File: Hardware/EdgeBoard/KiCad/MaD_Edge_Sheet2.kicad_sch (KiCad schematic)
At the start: 101 parts, among them IC1 ISO6742DWR, IC10 NSI50010YT1G, IC11 NSI50010YT1G, IC12 NSI50010YT1G, IC13 NSI50010YT1G, IC2 ISO6742DWR, IC3 UCC12040DVER, IC4 UCC12040DVER, IC5 ISO6731DWR, IC6 NSI50010YT1G, IC7 NSI50010YT1G, IC8 NSI50010YT1G, IC9 NSI50010YT1G, J10 ChargePump, J11 ESDUpper, J12 ESDLower, J13 ESDActive, J14 ENDUpper, J15 ENDLower, J16 Door, J17 GPI_3, J18 GPI_4, J19 NavKey, J4 436500321, J5 GPO_2, J6 GPO_1, J7 GPI_2, J8 GPI_1, J9 Force, U10 SN74LVC1G14DBV, U11 SN74LVC1G14DBV, U12 SN74LVC1G14DBV, U13 SN74LVC1G14DBV, U14 SN74LVC1G14DBV, U15 SN74LVC1G14DBV, U16 SN74LVC1G14DBV, U17 SN74LVC1G14DBV, U18 SN74LVC1G14DBV, U19 SN74LVC1G14DBV, U21 SN74LVC1G14DBV, U22 SN74LVC1G14DBV, U4 6N137, U5 VO2631, U6 VO2631, U7 VO2631, U8 VO2631, U9 SN74LVC1G14DBV

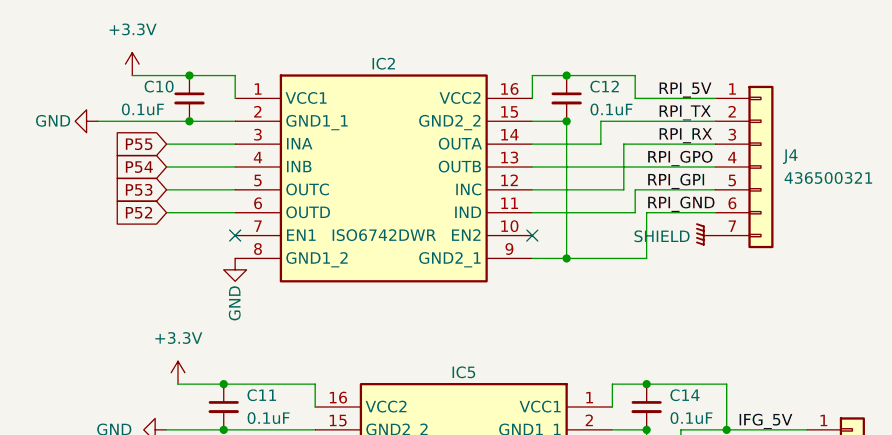
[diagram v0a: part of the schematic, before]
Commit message: fix(hardware): Pi link on P29-P32 and a 3.3 V Pi side
Findings HOST-F2 and HOST-F5. The P2-EC32MB does not bring out P40-P57
(fingers 59-62 are no-connects), so IC2 on P52-P55 was dead, and the Pi
side ran from 5 V, putting about 5 V on Pi GPIO.

- IC2 INA/INB/OUTC/OUTD move to P32/P31/P30/P29. P29-P31 are the only
  EC32MB pins the carrier leaves unused; the fourth (an isolator input,
  10 uA max, SLLSFJ6G p.12) shares P32 with J22.3.
- Routes: the old P52-P55 copper is removed; IC2 to four vias, B.Cu down
  to J22.3 (P32) and to vias in J3 fingers 9-11 (the only access).
- RPI_5V renamed RPI_3V3 (pads, tracks, In2 plane); J4.1 silkscreen
  reads 3V3. ISO674x runs at 2.25-5.5 V with VIT+ = 0.7 VCCI (SLLSFJ6G
  p.8, p.12).
- IC2 alternate ISO7742FDWR dropped: a default-low output would hold the
  UART low (SLLSFJ6G p.31).

Firmware follow-up: HW_PIN_RPI_TX 55 -> 32, HW_PIN_RPI_RX 53 -> 30.

Co-Authored-By: Claude Opus 5.5 <noreply@anthropic.com>
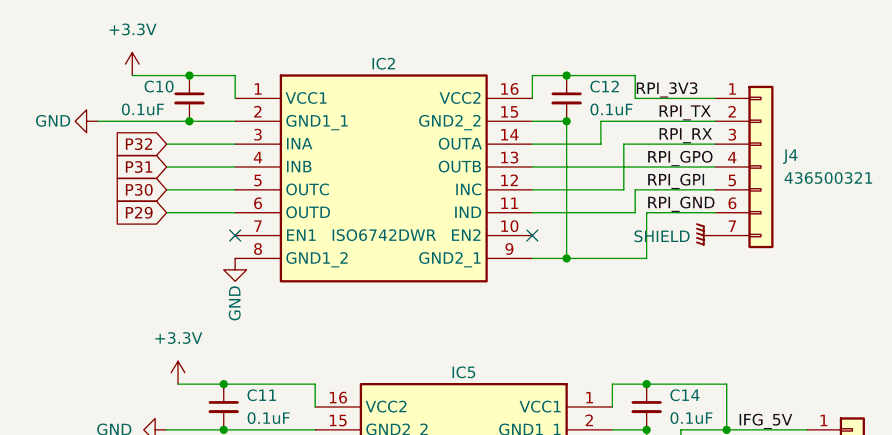
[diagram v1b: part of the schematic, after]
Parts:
- IC2: NOTES Pin Compatible with ISO77xx -> Non-F (default-high) part only: UART lines idle high. VCC2 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; manufacturer_part_number_1 ISO6742DWR or ISO7742FDWR -> ISO6742DWR
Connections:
- net P52 renamed P29
- net P53 renamed P30
- net P54 renamed P31
- net P55 renamed P32
- net RPI_5V renamed RPI_3V3
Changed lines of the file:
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@@
 		)
 	)
-	(label "RPI_5V"
-		(at 85.09 21.59 0)
+	(label "RPI_3V3"
+		(at 82.55 21.59 0)
 		(effects
 			(font
@@
 		)
 	)
-	(global_label "P52"
+	(global_label "P29"
 		(shape input)
 		(at 30.48 34.29 180)
@@
 		)
 	)
-	(global_label "P54"
+	(global_label "P31"
 		(shape input)
 		(at 30.48 29.21 180)
@@
 		)
 	)
-	(global_label "P55"
+	(global_label "P32"
 		(shape input)
 		(at 30.48 26.67 180)
@@
 		)
 	)
-	(global_label "P53"
+	(global_label "P30"
 		(shape input)
 		(at 30.48 31.75 180)
@@
 			)
 		)
-		(property "NOTES" "Pin Compatible with ISO77xx"
+		(property "NOTES" "Non-F (default-high) part only: UART lines idle high. VCC2 = RPI_3V3 from the Pi 3.3 V pin (VCC 2.25-5.5 V, SLLSFJ6G)."
 			(at 38.1 21.59 0)
 			(effects
@@
 			)
 		)
-		(property "manufacturer_part_number_1" "ISO6742DWR or ISO7742FDWR"
+		(property "manufacturer_part_number_1" "ISO6742DWR"
 			(at 38.1 21.59 0)
 			(effects

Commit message: fix(hardware): J4 back on the 43045-0618 footprint
Finding HOST-J4. J4's BOM part is 0430450618 (with solder tabs) and the
2023 board used the 43045-0618 footprint; the current files had 0615
(no tabs). The library footprint drops in at the same place: its two
mounting pads clear all copper (checked against every F.Cu item with
0.2 mm clearance). The tabs stay unnumbered as in 2023, so the DRC
parity note about J4 pin 7 (SHIELD) is unchanged.

Co-Authored-By: Claude Opus 5.5 <noreply@anthropic.com>
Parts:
- J4: footprint Connector_Molex:Molex_Micro-Fit_3.0_43045-0615_2x03_P3.00mm_Vertical -> Connector_Molex:Molex_Micro-Fit_3.0_43045-0618_2x03-1MP_P3.00mm_Vertical
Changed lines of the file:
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@@
 			)
 		)
-		(property "Footprint" "Connector_Molex:Molex_Micro-Fit_3.0_43045-0615_2x03_P3.00mm_Vertical"
+		(property "Footprint" "Connector_Molex:Molex_Micro-Fit_3.0_43045-0618_2x03-1MP_P3.00mm_Vertical"
 			(at 96.52 29.21 0)
 			(effects

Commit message: docs(hardware): Edge carrier revision v0.3: marking and changelog
- Title blocks (three sheets and the PCB) and the silkscreen read v0.3.
- readme: the v0.3 changelog (each change, the finding, the datasheet
  cite), encoder jumper settings for RS-422, open-collector and push-pull
  encoders, the supported loop range, J1 as the host port, the P2-EC32MB
  pin facts, the J3 via-in-pad fab note, and the firmware/SIL follow-up.

Co-Authored-By: Claude Opus 5.5 <noreply@anthropic.com>
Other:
- company: (none) -> MaD
- title: (none) -> MaD Edge carrier: I/O and host link
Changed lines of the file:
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@@
 	(generator_version "9.0")
 	(paper "A4")
+	(title_block
+		(title "MaD Edge carrier: I/O and host link")
+		(date "2026-10-25")
+		(rev "v0.3")
+		(company "MaD")
+		(comment 1 "Revision v0.3: fixes from the SIL hardware findings; see Hardware/EdgeBoard/readme.md")
+	)
 	(text "5V"
 		(exclude_from_sim no)

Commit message: fix(hardware): IC1/IC2 order the non-F ISO6742DWR (LCSC C5216407)
Both isolators carried LCSC C2862403, which LCSC's product detail lists as
the ISO7742FDWR (measured). That is the default-low F part: on IC2 it would
hold the Pi's RX low (a break) whenever the P2 is in reset or not driving
P32, and hold P30 low with no Pi attached (SLLSFJ6G function table).

C5216407 is the TI ISO6742DWR (LCSC product detail, measured), the part
both symbols are drawn as and the one the DigiKey number names. IC1 follows
IC2 into the same row and drops its ISO7742FDWR alternate. The firmware
does not drive P24-P27 (no HW_pins.h entry), so IC1's outputs change only
in what an unused channel idles at.

Fields only; no connectivity change.

Co-Authored-By: Claude Opus 5.5 <noreply@anthropic.com>
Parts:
- IC1: LCSC C2862403 -> C5216407; NOTES Pin Compatible with ISO77xx -> Pin compatible with ISO77xx. Ordered as the non-F ISO6742DW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; manufacturer_part_number_1 ISO6742DWR or ISO7742FDWR -> ISO6742DWR
- IC2: LCSC C2862403 -> C5216407
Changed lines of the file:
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@@
 			)
 		)
-		(property "LCSC" "C2862403"
+		(property "LCSC" "C5216407"
 			(at 38.1 21.59 0)
 			(effects
@@
 			)
 		)
-		(property "LCSC" "C2862403"
+		(property "LCSC" "C5216407"
 			(at 36.83 134.62 0)
 			(effects
@@
 			)
 		)
-		(property "NOTES" "Pin Compatible with ISO77xx"
+		(property "NOTES" "Pin compatible with ISO77xx. Ordered as the non-F ISO6742DWR (LCSC C5216407): outputs idle high while the input side is unpowered or undriven (SLLSFJ6G)."
 			(at 36.83 134.62 0)
 			(effects
@@
 			)
 		)
-		(property "manufacturer_part_number_1" "ISO6742DWR or ISO7742FDWR"
+		(property "manufacturer_part_number_1" "ISO6742DWR"
 			(at 36.83 134.62 0)
 			(effects

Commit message: fix(hardware): BOM fields for F1, the 0.1 uF row, the shunts and J25
- F1: LCSC C7542932 is the LUTE 1206L020/30NR (LCSC product detail,
  measured): 0.20 A hold, 0.46 A trip, 30 V (LUTE 1206L datasheet, Revision
  2020, p.2). Manufacturer, trip current and datasheet link now say so.
- The 0.1 uF 0603 row (22 parts, C31 among them) orders LCSC C14663, the
  YAGEO CC0603KRX7R9BB104, 50 V X7R 0603 (LCSC product detail, measured).
  Its primary MPN was a Samsung 0402 part (CL05A104KA5NNNC) with a 6 V
  description. The MPN, manufacturer and description now match the ordered
  part; the DigiKey number that went with the Samsung MPN is cleared
  because it could not be checked.
- SH1-SH4: noted as hand-fit after assembly (no footprint, no CPL entry).
- IC14: note to check the ISO7741F top marking on receipt (SLLSEP4K
  package addendum p.38), since LCSC's parametric text for C485810 calls
  its fail-safe state high.
- J25: VIN is the encoder's own rated supply, 30 V max (F1), isolated from
  V_IN.

Fields only; no connectivity change.

Co-Authored-By: Claude Opus 5.5 <noreply@anthropic.com>
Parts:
- C10, C11, C12, C13, C14, C15, C18, C19, C20, C21, C22, C23, C7, C8, C9: DIGIKEY 1276-1043-1-ND -> (none); MANUFACTURER Samsung Electro-Mechanics -> YAGEO; Manufacturer_Part_Number CL05A104KA5NNNC -> CC0603KRX7R9BB104
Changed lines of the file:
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@@
 			)
 		)
-		(property "Description" "0.1uF 6V SMD"
+		(property "Description" "0.1uF 50V X7R 0603"
 			(at 29.21 171.45 0)
 			(effects
@@
 			)
 		)
-		(property "MANUFACTURER" "Samsung Electro-Mechanics"
+		(property "MANUFACTURER" "YAGEO"
 			(at 29.21 171.45 0)
 			(effects
@@
 			)
 		)
-		(property "Manufacturer_Part_Number" "CL05A104KA5NNNC"
+		(property "Manufacturer_Part_Number" "CC0603KRX7R9BB104"
 			(at 29.21 171.45 0)
 			(effects
@@
 			)
 		)
-		(property "DIGIKEY" "1276-1043-1-ND"
+		(property "DIGIKEY" ""
 			(at 29.21 171.45 0)
 			(effects
@@
 			)
 		)
-		(property "Description" "0.1uF 6V SMD"
+		(property "Description" "0.1uF 50V X7R 0603"
 			(at 83.82 81.28 0)
 			(effects
@@
 			)
 		)
-		(property "MANUFACTURER" "Samsung Electro-Mechanics"
+		(property "MANUFACTURER" "YAGEO"
 			(at 83.82 81.28 0)
 			(effects
@@
 			)
 		)
-		(property "Manufacturer_Part_Number" "CL05A104KA5NNNC"
+		(property "Manufacturer_Part_Number" "CC0603KRX7R9BB104"
 			(at 83.82 81.28 0)
 			(effects
@@
 			)
 		)
-		(property "DIGIKEY" "1276-1043-1-ND"
+		(property "DIGIKEY" ""
 			(at 83.82 81.28 0)
 			(effects
@@
 			)
 		)
-		(property "Description" "0.1uF 6V SMD"
+		(property "Description" "0.1uF 50V X7R 0603"
 			(at 97.79 176.53 0)
 			(effects
@@
 			)
 		)
-		(property "MANUFACTURER" "Samsung Electro-Mechanics"
+		(property "MANUFACTURER" "YAGEO"
 			(at 97.79 176.53 0)
 			(effects
@@
 			)
 		)
-		(property "Manufacturer_Part_Number" "CL05A104KA5NNNC"
+		(property "Manufacturer_Part_Number" "CC0603KRX7R9BB104"
 			(at 97.79 176.53 0)
 			(effects
@@
 			)
 		)
-		(property "DIGIKEY" "1276-1043-1-ND"
+		(property "DIGIKEY" ""
 			(at 97.79 176.53 0)
 			(effects
@@
 			)
 		)
-		(property "Description" "0.1uF 6V SMD"
+		(property "Description" "0.1uF 50V X7R 0603"
 			(at 154.94 20.32 0)
 			(effects
@@
 			)
 		)
-		(property "MANUFACTURER" "Samsung Electro-Mechanics"
+		(property "MANUFACTURER" "YAGEO"
 			(at 154.94 20.32 0)
 			(effects
@@
 			)
 		)
-		(property "Manufacturer_Part_Number" "CL05A104KA5NNNC"
+		(property "Manufacturer_Part_Number" "CC0603KRX7R9BB104"
 			(at 154.94 20.32 0)
 			(effects
@@
 			)
 		)
-		(property "DIGIKEY" "1276-1043-1-ND"
+		(property "DIGIKEY" ""
 			(at 154.94 20.32 0)
 			(effects
@@
 			)
 		)
-		(property "Description" "0.1uF 6V SMD"
+		(property "Description" "0.1uF 50V X7R 0603"
 			(at 154.94 58.42 0)
 			(effects
@@
 			)
 		)
-		(property "MANUFACTURER" "Samsung Electro-Mechanics"
+		(property "MANUFACTURER" "YAGEO"
 			(at 154.94 58.42 0)
 			(effects
@@
 			)
 		)
-		(property "Manufacturer_Part_Number" "CL05A104KA5NNNC"
+		(property "Manufacturer_Part_Number" "CC0603KRX7R9BB104"
 			(at 154.94 58.42 0)
 			(effects
@@
 			)
 		)
-		(property "DIGIKEY" "1276-1043-1-ND"
+		(property "DIGIKEY" ""
 			(at 154.94 58.42 0)
 			(effects
@@
 			)
 		)
-		(property "Description" "0.1uF 6V SMD"
+		(property "Description" "0.1uF 50V X7R 0603"
 			(at 78.74 134.62 0)
 			(effects
@@
 			)
 		)
-		(property "MANUFACTURER" "Samsung Electro-Mechanics"
+		(property "MANUFACTURER" "YAGEO"
 			(at 78.74 134.62 0)
 			(effects
@@
 			)
 		)
-		(property "Manufacturer_Part_Number" "CL05A104KA5NNNC"
+		(property "Manufacturer_Part_Number" "CC0603KRX7R9BB104"
 			(at 78.74 134.62 0)
 			(effects
@@
 			)
 		)
-		(property "DIGIKEY" "1276-1043-1-ND"
+		(property "DIGIKEY" ""
 			(at 78.74 134.62 0)
 			(effects
@@
 			)
 		)
-		(property "Description" "0.1uF 6V SMD"
+		(property "Description" "0.1uF 50V X7R 0603"
 			(at 36.83 55.88 0)
 			(effects
@@
 			)
 		)
-		(property "MANUFACTURER" "Samsung Electro-Mechanics"
+		(property "MANUFACTURER" "YAGEO"
 			(at 36.83 55.88 0)
 			(effects
@@
 			)
 		)
-		(property "Manufacturer_Part_Number" "CL05A104KA5NNNC"
+		(property "Manufacturer_Part_Number" "CC0603KRX7R9BB104"
 			(at 36.83 55.88 0)
 			(effects
@@
 			)
 		)
-		(property "DIGIKEY" "1276-1043-1-ND"
+		(property "DIGIKEY" ""
 			(at 36.83 55.88 0)
 			(effects
@@
 			)
 		)
-		(property "Description" "0.1uF 6V SMD"
+		(property "Description" "0.1uF 50V X7R 0603"
 			(at 31.75 90.17 0)
 			(effects
@@
 			)
 		)
-		(property "MANUFACTURER" "Samsung Electro-Mechanics"
+		(property "MANUFACTURER" "YAGEO"
 			(at 31.75 90.17 0)
 			(effects
@@
 			)
 		)
-		(property "Manufacturer_Part_Number" "CL05A104KA5NNNC"
+		(property "Manufacturer_Part_Number" "CC0603KRX7R9BB104"
 			(at 31.75 90.17 0)
 			(effects
@@
 			)
 		)
-		(property "DIGIKEY" "1276-1043-1-ND"
+		(property "DIGIKEY" ""
 			(at 31.75 90.17 0)
 			(effects
@@
 			)
 		)
-		(property "Description" "0.1uF 6V SMD"
+		(property "Description" "0.1uF 50V X7R 0603"
 			(at 74.93 21.59 0)
 			(effects
@@
 			)
 		)
-		(property "MANUFACTURER" "Samsung Electro-Mechanics"
+		(property "MANUFACTURER" "YAGEO"
 			(at 74.93 21.59 0)
 			(effects
@@
 			)
 		)
-		(property "Manufacturer_Part_Number" "CL05A104KA5NNNC"
+		(property "Manufacturer_Part_Number" "CC0603KRX7R9BB104"
 			(at 74.93 21.59 0)
 			(effects
@@
 			)
 		)
-		(property "DIGIKEY" "1276-1043-1-ND"
+		(property "DIGIKEY" ""
 			(at 74.93 21.59 0)
 			(effects
@@
 			)
 		)
-		(property "Description" "0.1uF 6V SMD"
+		(property "Description" "0.1uF 50V X7R 0603"
 			(at 31.75 134.62 0)
 			(effects
@@
 			)
 		)
-		(property "MANUFACTURER" "Samsung Electro-Mechanics"
+		(property "MANUFACTURER" "YAGEO"
 			(at 31.75 134.62 0)
 			(effects
@@
 			)
 		)
-		(property "Manufacturer_Part_Number" "CL05A104KA5NNNC"
+		(property "Manufacturer_Part_Number" "CC0603KRX7R9BB104"
 			(at 31.75 134.62 0)
 			(effects
@@
 			)
 		)
-		(property "DIGIKEY" "1276-1043-1-ND"
+		(property "DIGIKEY" ""
 			(at 31.75 134.62 0)
 			(effects
@@
 			)
 		)
-		(property "Description" "0.1uF 6V SMD"
+		(property "Description" "0.1uF 50V X7R 0603"
 			(at 83.82 55.88 0)
 			(effects
@@
 			)
 		)
-		(property "MANUFACTURER" "Samsung Electro-Mechanics"
+		(property "MANUFACTURER" "YAGEO"
 			(at 83.82 55.88 0)
 			(effects
@@
 			)
 		)
-		(property "Manufacturer_Part_Number" "CL05A104KA5NNNC"
+		(property "Manufacturer_Part_Number" "CC0603KRX7R9BB104"
 			(at 83.82 55.88 0)
 			(effects
@@
 			)
 		)
-		(property "DIGIKEY" "1276-1043-1-ND"
+		(property "DIGIKEY" ""
 			(at 83.82 55.88 0)
 			(effects
@@
 			)
 		)
-		(property "Description" "0.1uF 6V SMD"
+		(property "Description" "0.1uF 50V X7R 0603"
 			(at 133.35 182.88 0)
 			(effects
@@
 			)
 		)
-		(property "MANUFACTURER" "Samsung Electro-Mechanics"
+		(property "MANUFACTURER" "YAGEO"
 			(at 133.35 182.88 0)
 			(effects
@@
 			)
 		)
-		(property "Manufacturer_Part_Number" "CL05A104KA5NNNC"
+		(property "Manufacturer_Part_Number" "CC0603KRX7R9BB104"
 			(at 133.35 182.88 0)
 			(effects
@@
 			)
 		)
-		(property "DIGIKEY" "1276-1043-1-ND"
+		(property "DIGIKEY" ""
 			(at 133.35 182.88 0)
 			(effects
@@
 			)
 		)
-		(property "Description" "0.1uF 6V SMD"
+		(property "Description" "0.1uF 50V X7R 0603"
 			(at 154.94 96.52 0)
 			(effects
@@
 			)
 		)
-		(property "MANUFACTURER" "Samsung Electro-Mechanics"
+		(property "MANUFACTURER" "YAGEO"
 			(at 154.94 96.52 0)
 			(effects
@@
 			)
 		)
-		(property "Manufacturer_Part_Number" "CL05A104KA5NNNC"
+		(property "Manufacturer_Part_Number" "CC0603KRX7R9BB104"
 			(at 154.94 96.52 0)
 			(effects
@@
 			)
 		)
-		(property "DIGIKEY" "1276-1043-1-ND"
+		(property "DIGIKEY" ""
 			(at 154.94 96.52 0)
 			(effects
@@
 			)
 		)
-		(property "Description" "0.1uF 6V SMD"
+		(property "Description" "0.1uF 50V X7R 0603"
 			(at 154.94 134.62 0)
 			(effects
@@
 			)
 		)
-		(property "MANUFACTURER" "Samsung Electro-Mechanics"
+		(property "MANUFACTURER" "YAGEO"
 			(at 154.94 134.62 0)
 			(effects
@@
 			)
 		)
-		(property "Manufacturer_Part_Number" "CL05A104KA5NNNC"
+		(property "Manufacturer_Part_Number" "CC0603KRX7R9BB104"
 			(at 154.94 134.62 0)
 			(effects
@@
 			)
 		)
-		(property "DIGIKEY" "1276-1043-1-ND"
+		(property "DIGIKEY" ""
 			(at 154.94 134.62 0)
 			(effects
@@
 			)
 		)
-		(property "Description" "0.1uF 6V SMD"
+		(property "Description" "0.1uF 50V X7R 0603"
 			(at 33.02 21.59 0)
 			(effects
@@
 			)
 		)
-		(property "MANUFACTURER" "Samsung Electro-Mechanics"
+		(property "MANUFACTURER" "YAGEO"
 			(at 33.02 21.59 0)
 			(effects
@@
 			)
 		)
-		(property "Manufacturer_Part_Number" "CL05A104KA5NNNC"
+		(property "Manufacturer_Part_Number" "CC0603KRX7R9BB104"
 			(at 33.02 21.59 0)
 			(effects
@@
 			)
 		)
-		(property "DIGIKEY" "1276-1043-1-ND"
+		(property "DIGIKEY" ""
 			(at 33.02 21.59 0)
 			(effects
